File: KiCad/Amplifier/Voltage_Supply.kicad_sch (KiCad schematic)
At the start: 15 parts, among them J3 Molex_26013115, J4 Molex_26013115, J5 Molex_26013115

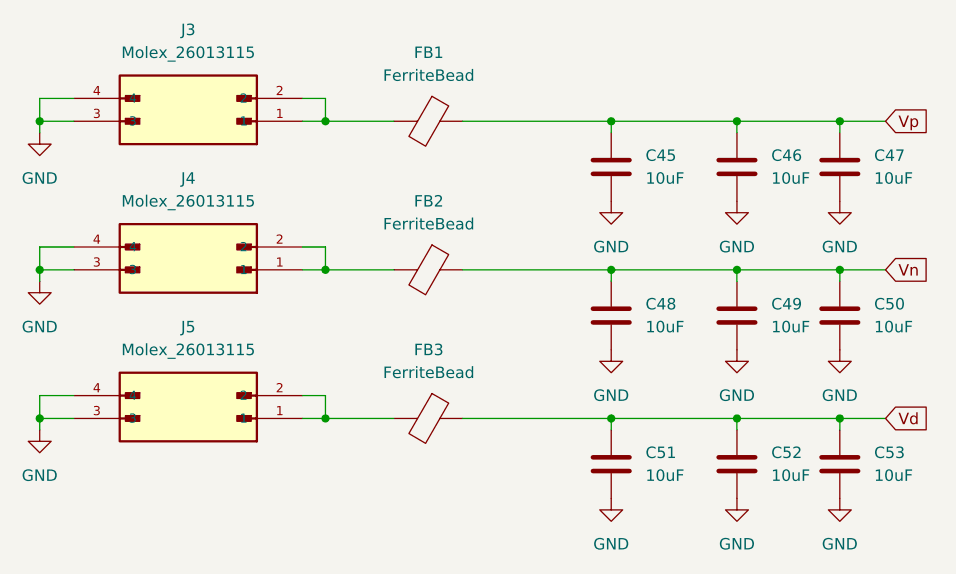
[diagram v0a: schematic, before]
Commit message: Platinenentwurf
die Platine wurde aufgebaut. Kontrolle fehlt
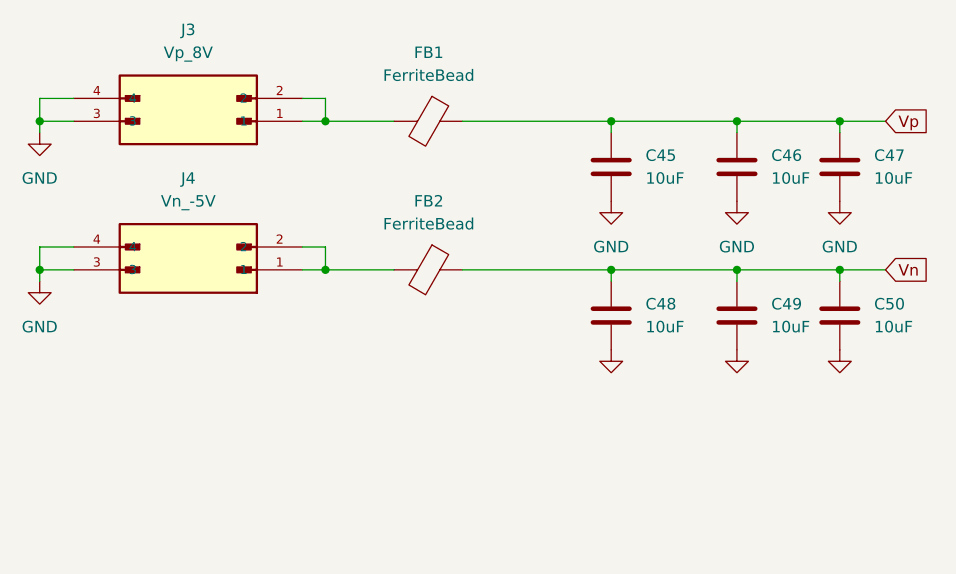
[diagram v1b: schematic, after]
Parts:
- removed C51, C52, C53: 10uF, Capacitor_SMD:C_0603_1608Metric_Pad1.08x0.95mm_HandSolder, symbol Device:C
- removed FB3: FerriteBead, Library:BLM21PG300SN1B, symbol Device:FerriteBead
- removed J5: Molex_26013115, Library:MOLEX_26013115, symbol New_Library_0:Molex_26013115
- C45, C46, C47, C48, C49, C50: footprint Capacitor_SMD:C_0603_1608Metric_Pad1.08x0.95mm_HandSolder -> Capacitor_SMD:C_1210_3225Metric_Pad1.33x2.70mm_HandSolder
- J3: value Molex_26013115 -> Vp_8V
- J4: value Molex_26013115 -> Vn_-5V

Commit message: Update PCB
update PCB
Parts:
- removed J3: Vp_8V, Library:MOLEX_26013115, symbol New_Library_0:Molex_26013115
- removed J4: Vn_-5V, Library:MOLEX_26013115, symbol New_Library_0:Molex_26013115
- added J3: Vp_8V, Library:MOLEX_26013115, symbol Connector_Generic:Conn_02x02_Counter_Clockwise
- added J4: Vn_-5V, Library:MOLEX_26013115, symbol Connector_Generic:Conn_02x02_Counter_Clockwise
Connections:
- net GND: now also J3.3 (Pin_3), J3.4 (Pin_4), J4.3 (Pin_3), J4.4 (Pin_4)
- net at FB1.2: now also J3.1 (Pin_1), J3.2 (Pin_2)
- net at FB2.2: now also J4.1 (Pin_1), J4.2 (Pin_2)
